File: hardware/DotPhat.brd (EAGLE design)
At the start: 30 x 80.7 mm, 61 parts, among them CN1 1X4-BIG, IC1 CAT24M010TS, IC3 SI1145, J2 RASPBERRYPI-40-PIN-GPIO_PTH, J3 USB-MICROB, Q1 BSH103, U1 ATMEGA328P-MU-QFN32, U2 TMP102, U3 ATSHA204-TSU, U4 W25Q32FV, X2 MC-RTC-RV-4162-C7-I2C, X3 S4B-ZR

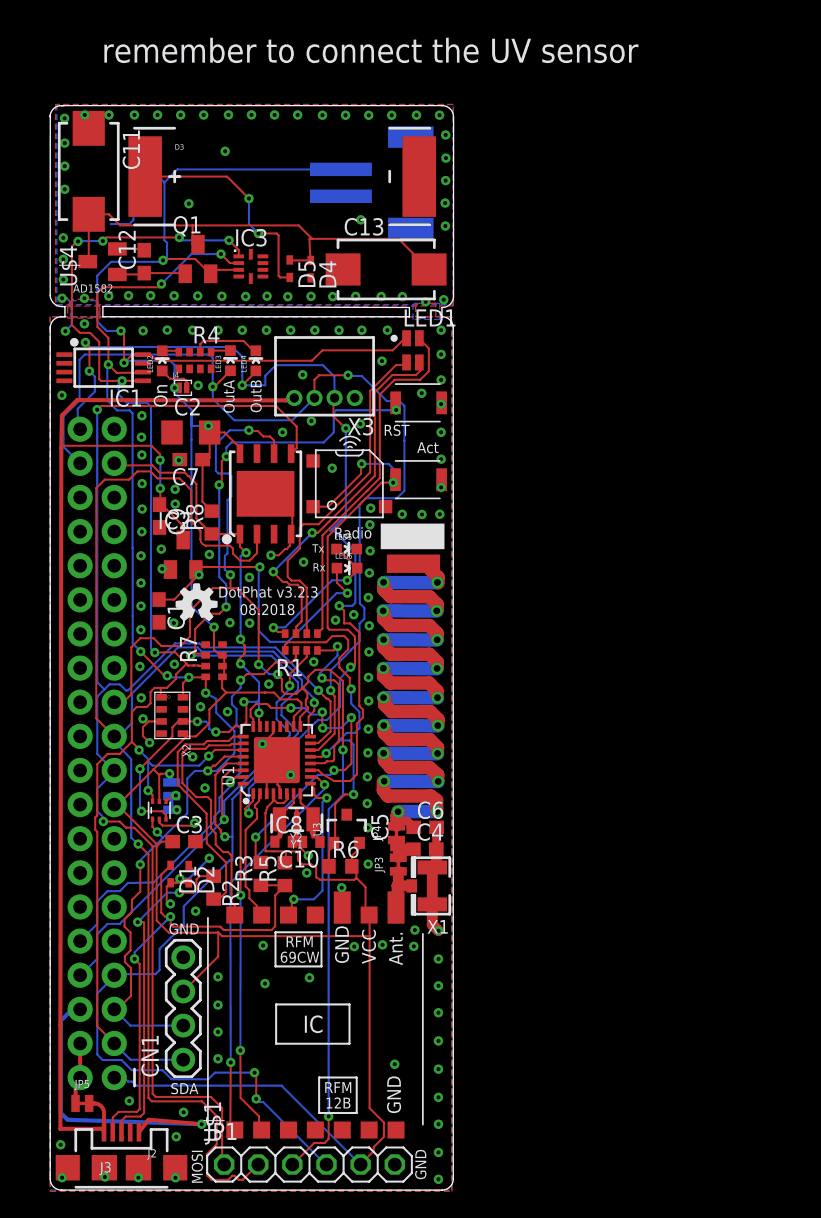
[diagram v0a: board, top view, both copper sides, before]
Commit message: Beta: initial arrange of solar
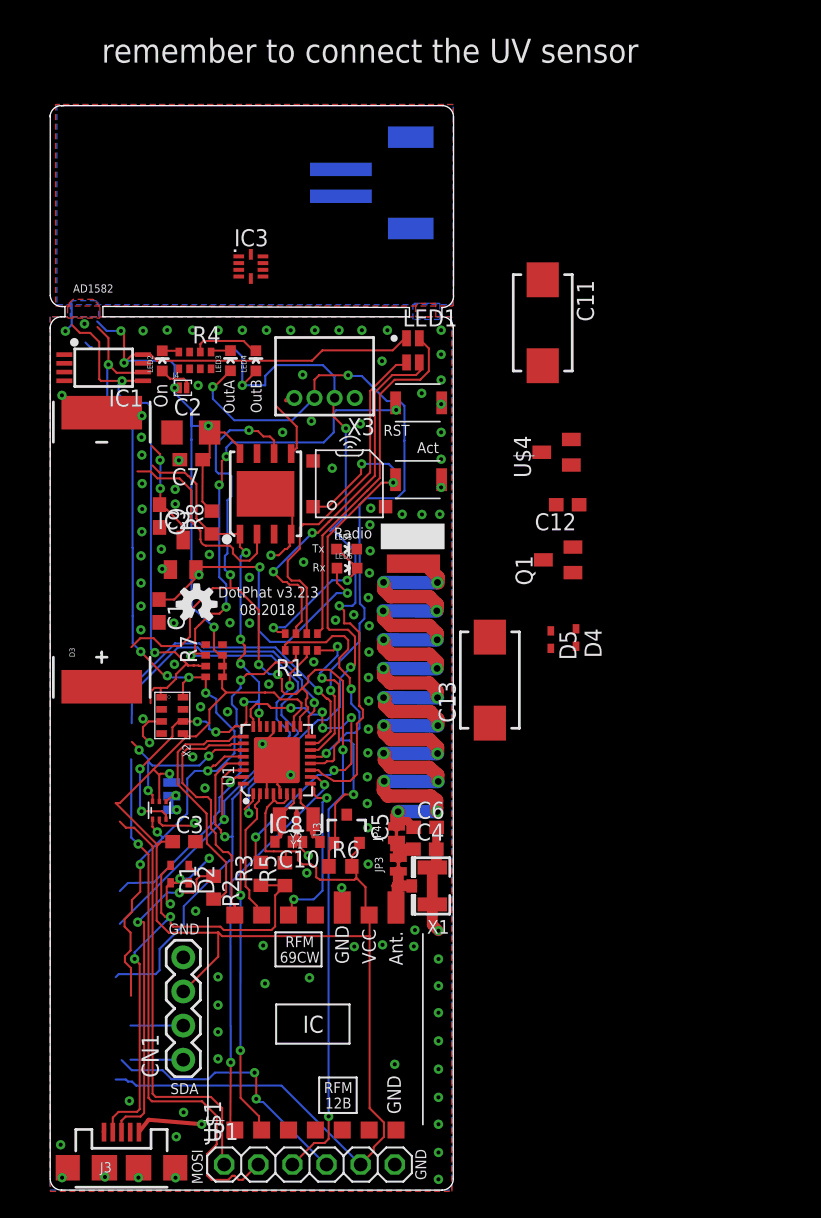
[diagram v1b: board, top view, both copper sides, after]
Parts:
- removed J2: RASPBERRYPI-40-PIN-GPIO_PTH, SparkFun-Connectors:2X20_SHROUDED
- removed JP5: JUMPER-SMT_2_NC_TRACE_NO-SILK, SparkFun-Jumpers:SMT-JUMPER_2_NC_TRACE_NO-SILK
- moved U$4 36.6 mm to (37.7, 54.9)
- moved C12 36.3 mm to (38.5, 51.0), turned to 180 degrees
- moved C11 35.6 mm to (36.7, 64.6)
- moved Q1 34.9 mm to (37.8, 46.9), turned to 90 degrees
- moved D4 33.8 mm to (39.1, 41.2)
- moved D5 33.8 mm to (37.3, 41.0)
- moved C13 31.5 mm to (32.7, 38.0), turned to 90 degrees
- moved D3 30.9 mm to (3.84, 47.7), turned to 90 degrees
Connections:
- removed net N$36: J2.2, J2.4, JP5.1
- net +3V3: no longer J2.1, J2.17
- net +5V: no longer JP5.2
- net CS_FLASH: no longer J2.37
- net GND: no longer J2.14, J2.20, J2.25, J2.30, J2.34, J2.39, J2.6, J2.9
- net MISO: no longer J2.21
- net MOSI: no longer J2.19
- net OUTA: no longer J2.38
- net OUTB: no longer J2.40
- net RST: no longer J2.7
- net RXD: no longer J2.8
- net SCK: no longer J2.23
- net SCL: no longer J2.5
- net SDA: no longer J2.3
- net TXD: no longer J2.10
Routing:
- net +5V: track 93.7 -> 10.6 mm
- net SDA: track 107.1 -> 57.4 mm, vias 9 -> 5
- net MOSI: track 107.5 -> 58.4 mm, vias 3 -> 1
- net +3V3: track 258.4 -> 215.8 mm, vias 10 -> 9
- net CAPS_VCC: track 35.8 -> 0.00 mm
- net MISO: track 105.1 -> 78.3 mm
- net GND: track 70.8 -> 48.2 mm, vias 173 -> 122
- net OUTA: track 72.5 -> 51.5 mm
- net SCL: track 93.4 -> 75.0 mm, vias 10 -> 8
- net OUTB: track 69.1 -> 51.0 mm, vias 5 -> 3
- net N$5: track 16.8 -> 0.00 mm, vias 2 -> 0
- net RST: track 109.4 -> 100.8 mm
- net RXD: track 37.5 -> 31.9 mm
- net SCK: track 91.5 -> 86.0 mm
- net TXD: track 33.1 -> 27.6 mm
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
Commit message: Reroute signals after repositioning
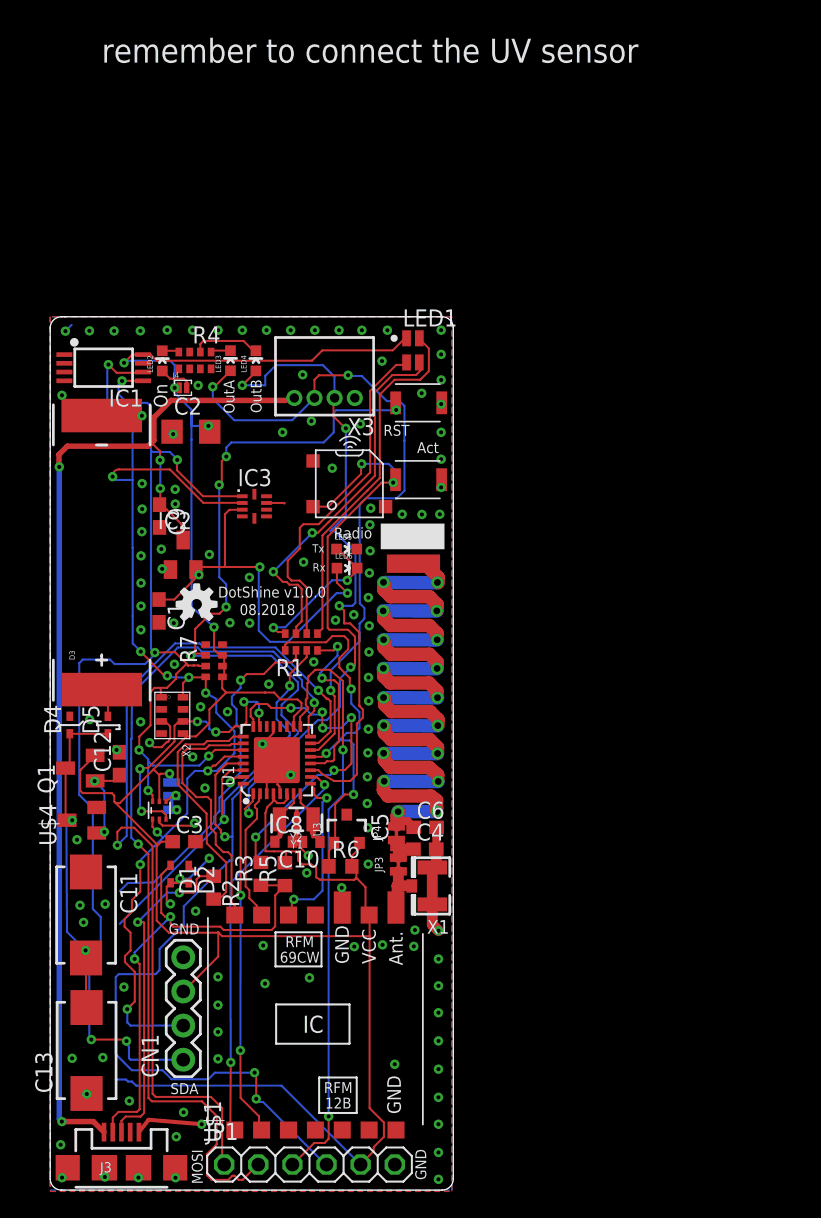
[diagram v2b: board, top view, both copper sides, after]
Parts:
- removed C7: (no value), rcl:C0603
- removed CN2: (no value), adafruit:JST-PH-2-SMT-RA
- removed R8: 1.5kΩ, rcl:R0603
- removed U4: W25Q32FV, SparkFun-IC-Memory:WSON8-6X5MM
- moved C11 55.7 mm to (2.67, 20.5)
- moved U$4 44.7 mm to (2.36, 27.5)
- moved C13 40.8 mm to (2.71, 10.4)
- moved Q1 38.8 mm to (2.25, 31.4)
- moved C12 38.5 mm to (5.16, 31.7), turned to 90 degrees
- moved D4 38.3 mm to (1.46, 34.6), turned to 90 degrees
- moved D5 33.6 mm to (4.30, 34.6), turned to 90 degrees
- moved IC3 17.9 mm to (15.2, 50.9)
- moved D3 0.21 mm to (3.84, 47.5)
- moved C2 0.06 mm to (10.5, 56.4)
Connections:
- net +3V3: no longer C7.1, CN2.1, R8.2, U4.8
- net CS_FLASH: no longer R8.1, U4.1
- net GND: no longer C7.2, CN2.2, U4.4
- net MISO: no longer U4.2
- net MOSI: no longer U4.5
- net SCK: no longer U4.6
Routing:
- net +5V: track 10.6 -> 83.6 mm, vias 2 -> 4
- net SDA: track 57.4 -> 101.7 mm, vias 5 -> 8
- net SCK: track 86.0 -> 45.2 mm, vias 6 -> 2
- net CAPS_VCC: track 0.00 -> 24.9 mm, vias 0 -> 2
- net CS_FLASH: track 45.0 -> 21.0 mm, vias 9 -> 6
- net MISO: track 78.3 -> 65.7 mm
- net SCL: track 75.0 -> 87.5 mm, vias 8 -> 10
- net MOSI: track 58.4 -> 67.0 mm, vias 1 -> 2
- net MOSFET: track 0.00 -> 6.72 mm, vias 0 -> 2
- net RST: track 100.8 -> 107.1 mm
- net GND: track 48.2 -> 42.0 mm, vias 122 -> 130
- net OUTB: track 51.0 -> 47.3 mm
- net +3V3: track 215.8 -> 213.3 mm, vias 9 -> 8
- net N$5: track 0.00 -> 2.18 mm
- removed copper zone on layer 1, net N$25
- removed copper zone on layer 16, net N$34
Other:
- board size 30 x 80.7 mm -> 30 x 65 mm
- board text added: "DotShine v1.0.0"
- board text removed: "AD1582"
- board text removed: "DotPhat v3.2.3"

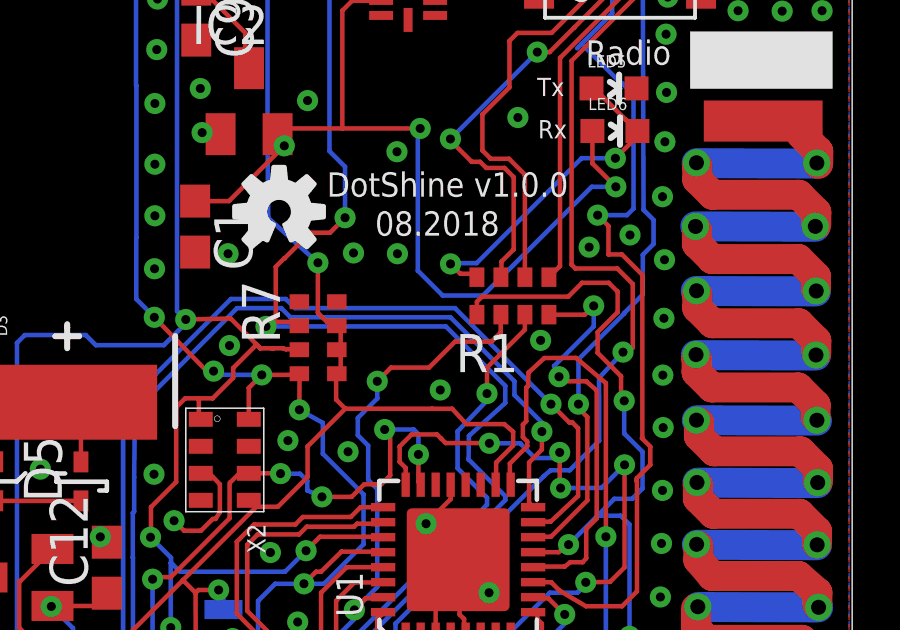
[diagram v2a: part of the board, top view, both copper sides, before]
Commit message: Add TP for TRx leds
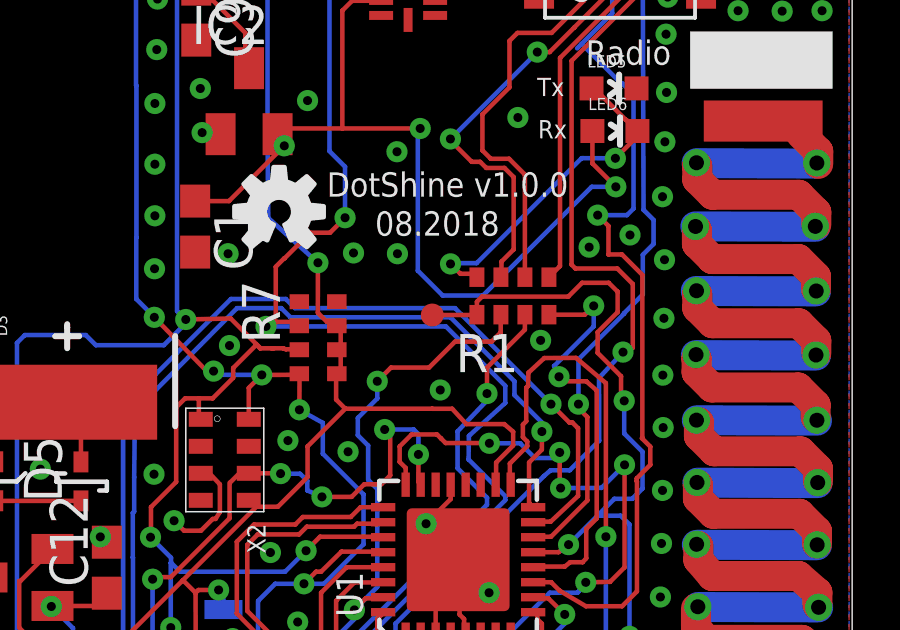
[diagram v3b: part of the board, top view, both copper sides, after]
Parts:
- added TP1: TEST-POINT3, SparkFun:PAD.03X.03
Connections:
- net ADCENA: now also TP1.P$1
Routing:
- net ADCENA: track 29.1 -> 30.6 mm
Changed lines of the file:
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@@
 <element name="C12" library="rcl" package="C0603" value="1uF 4V" x="5.158" y="31.734" rot="R90"/>
 <element name="IC3" library="silabs" package="QFN-10" value="SI1145" x="15.201" y="50.892"/>
+<element name="TP1" library="SparkFun" package="PAD.03X.03" value="TEST-POINT3" x="16.006" y="40.157"/>
 </elements>
 <signals>
@@
 <wire x1="17.665" y1="40.77" x2="17.4944" y2="40.5994" width="0.1524" layer="1"/>
 <wire x1="17.4944" y1="40.5994" x2="17.4944" y2="40.1674" width="0.1524" layer="1"/>
+<contactref element="TP1" pad="P$1"/>
+<wire x1="16.006" y1="40.157" x2="17.4944" y2="40.157" width="0.1524" layer="1"/>
+<wire x1="17.4944" y1="40.157" x2="17.4944" y2="40.1674" width="0.1524" layer="1"/>
 </signal>
 <signal name="MOSI">

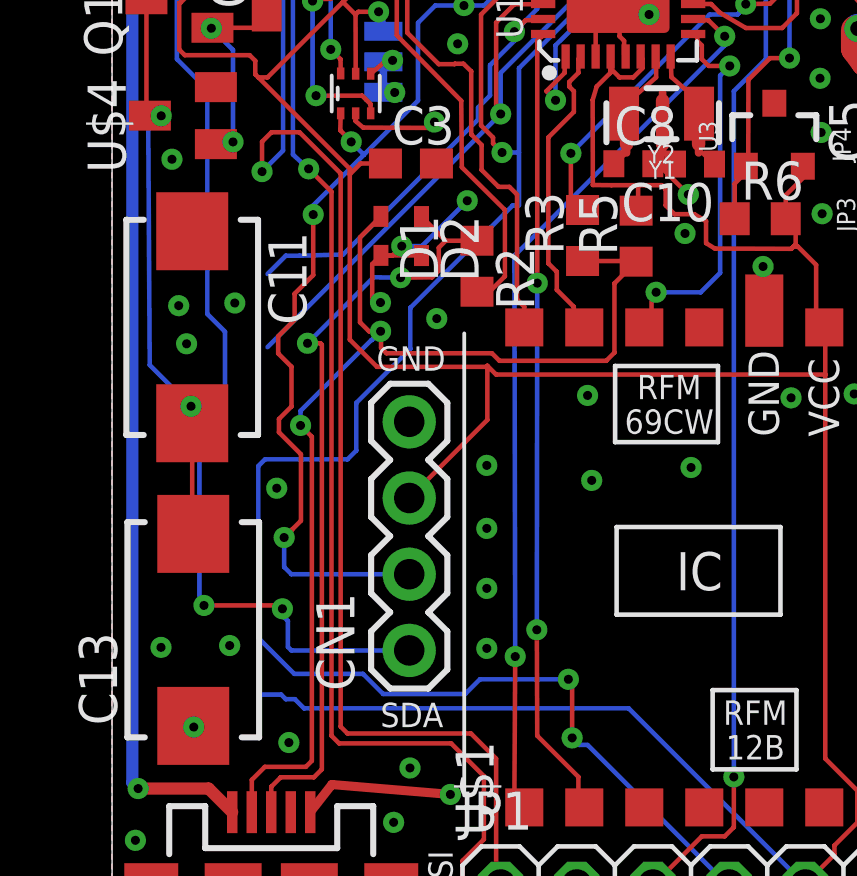
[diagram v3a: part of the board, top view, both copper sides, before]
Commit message: Reposition components to accomodate possible LoRA RF
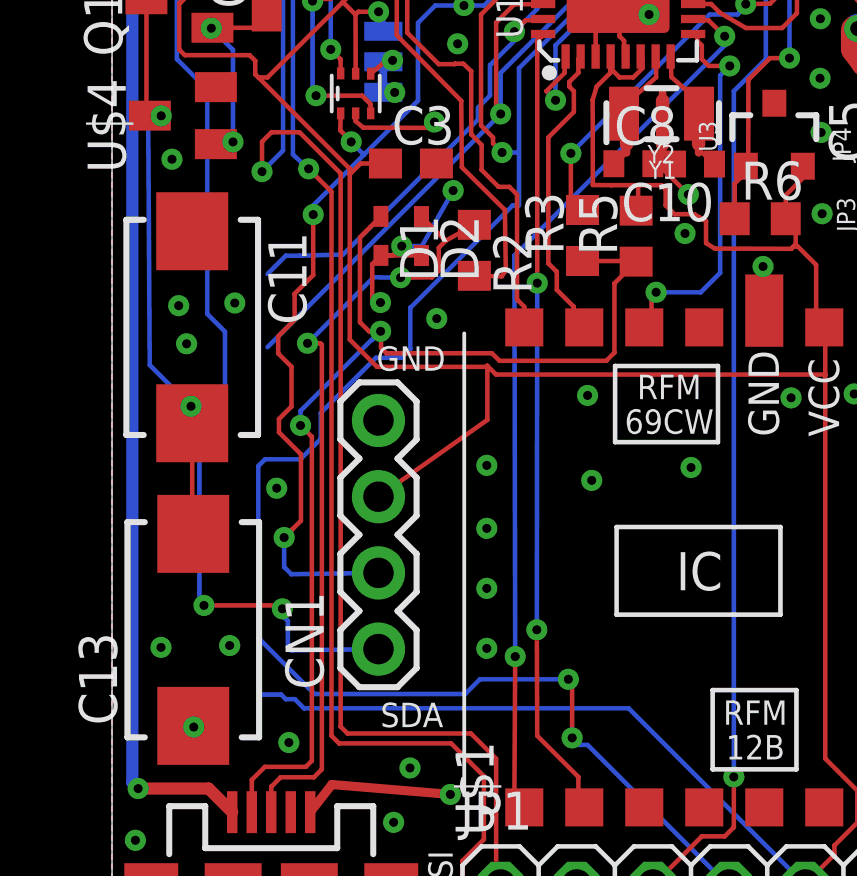
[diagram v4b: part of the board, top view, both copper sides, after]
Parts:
- moved CN1 1.03 mm to (8.88, 9.75)
- moved R2 0.54 mm to (12.1, 23.0)
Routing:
- net SDA: track 101.7 -> 100.6 mm
- net SCL: track 87.5 -> 86.4 mm
- net +3V3: track 213.3 -> 214.0 mm

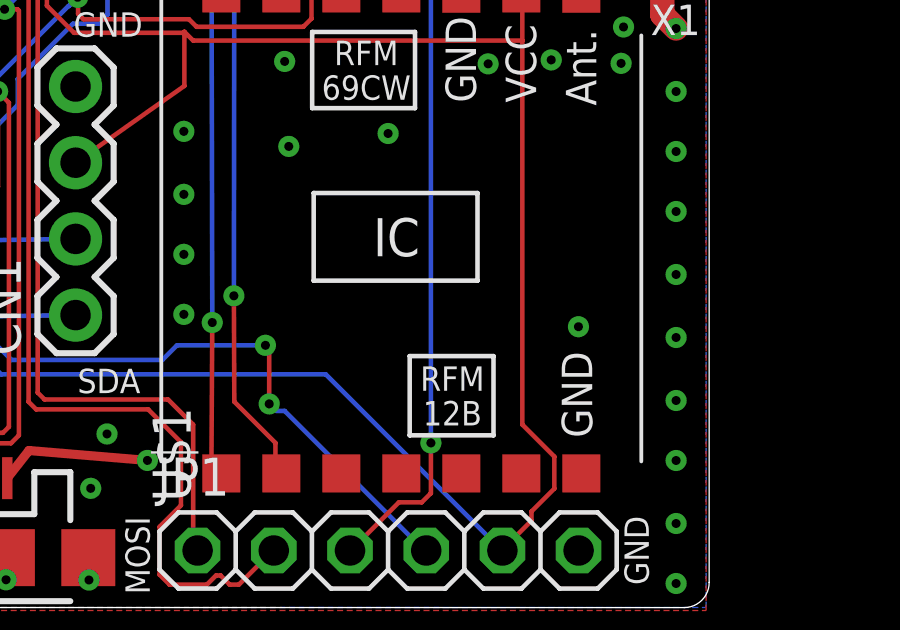
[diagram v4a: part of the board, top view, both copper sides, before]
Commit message: Add FSK/LoRA silkscreen
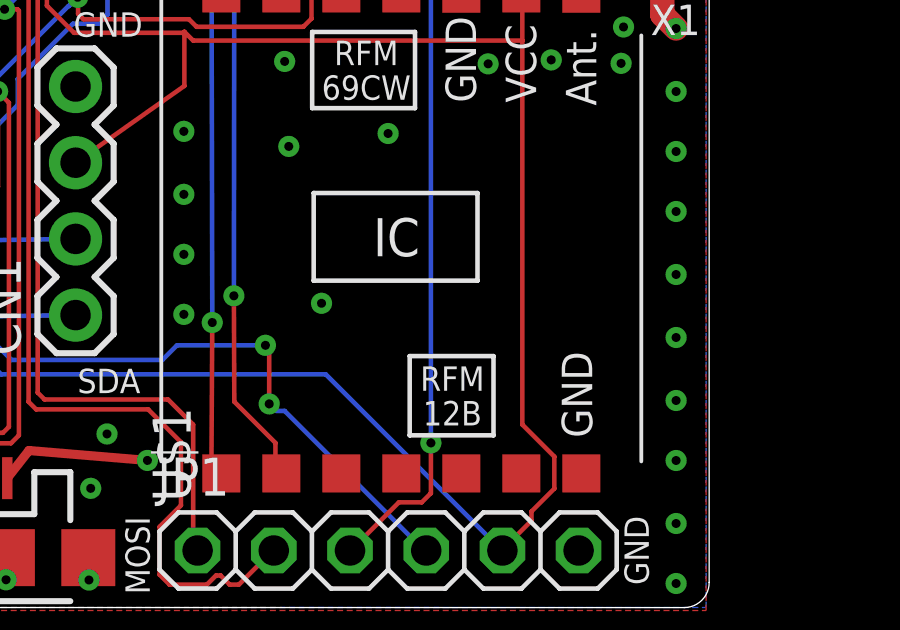
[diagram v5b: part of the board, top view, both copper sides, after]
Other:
- board text added: "FSK"
- board text added: "LoRA"
